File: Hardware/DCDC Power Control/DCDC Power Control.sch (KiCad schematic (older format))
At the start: 33 parts, among them J1 Conn_01x03, J2 Conn_01x02, J3 Conn_01x02, J4 Screw_Terminal_01x02, J5 Conn_01x01, Q2 SQJ479EP-T1_GE3, U1 CPC2025N

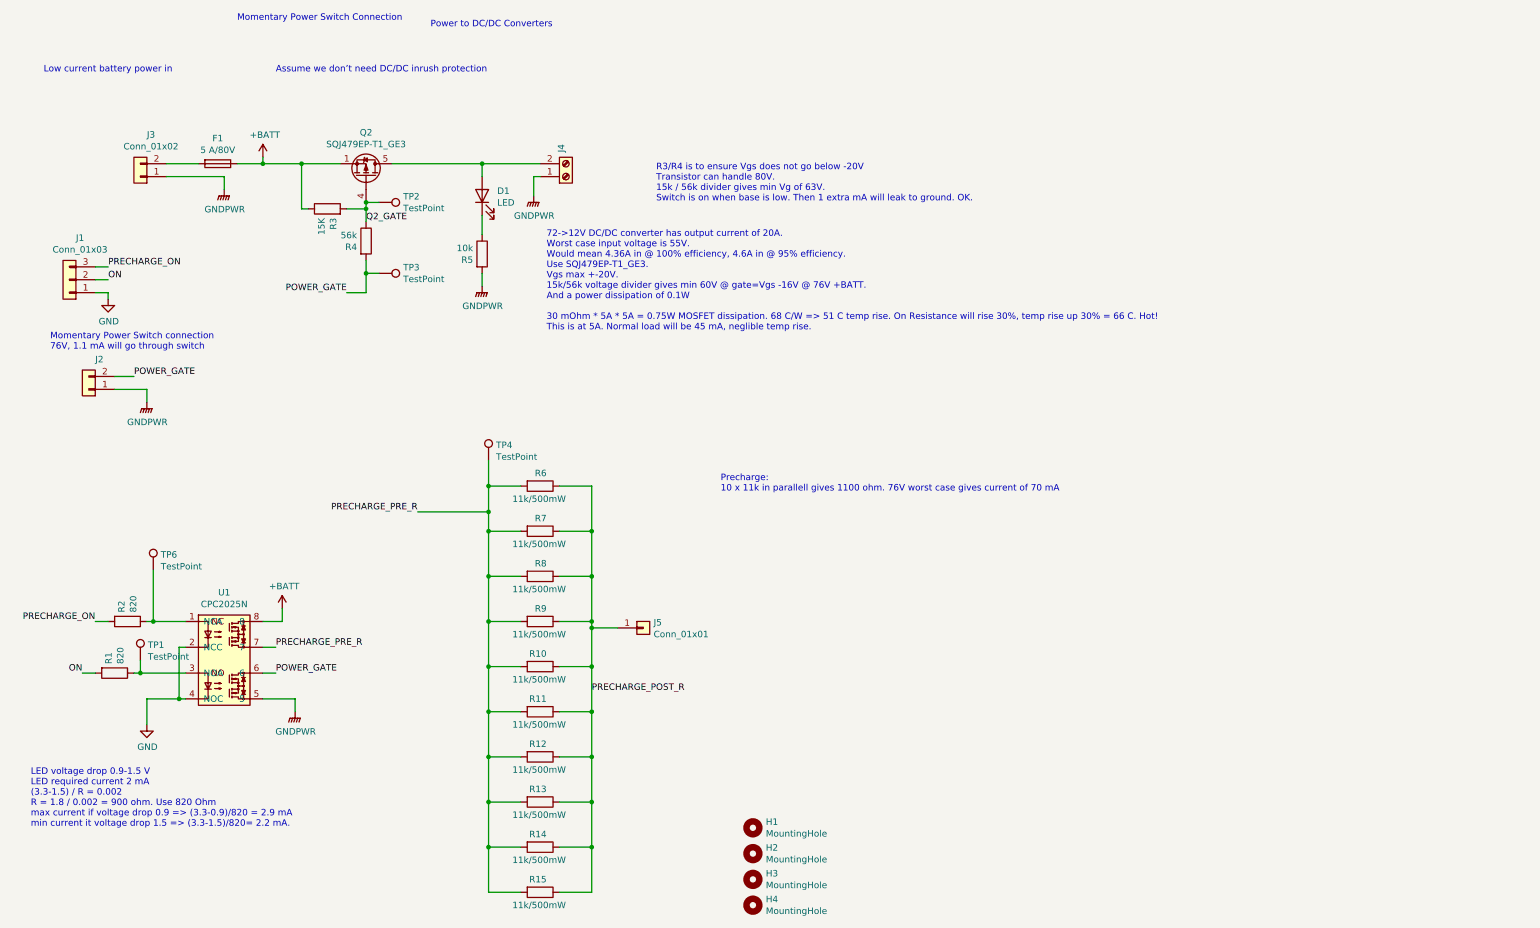
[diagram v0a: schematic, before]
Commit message: Revision 2 of the DCDC Control PCB.
Now with precharge for both DC/DC and VESC, 150 ohm 45 W precharge resistors
(up to three per device).

Microcontroller to control the sequencing. ADC measurement of in vs out voltage
to determine when precharge is complete.
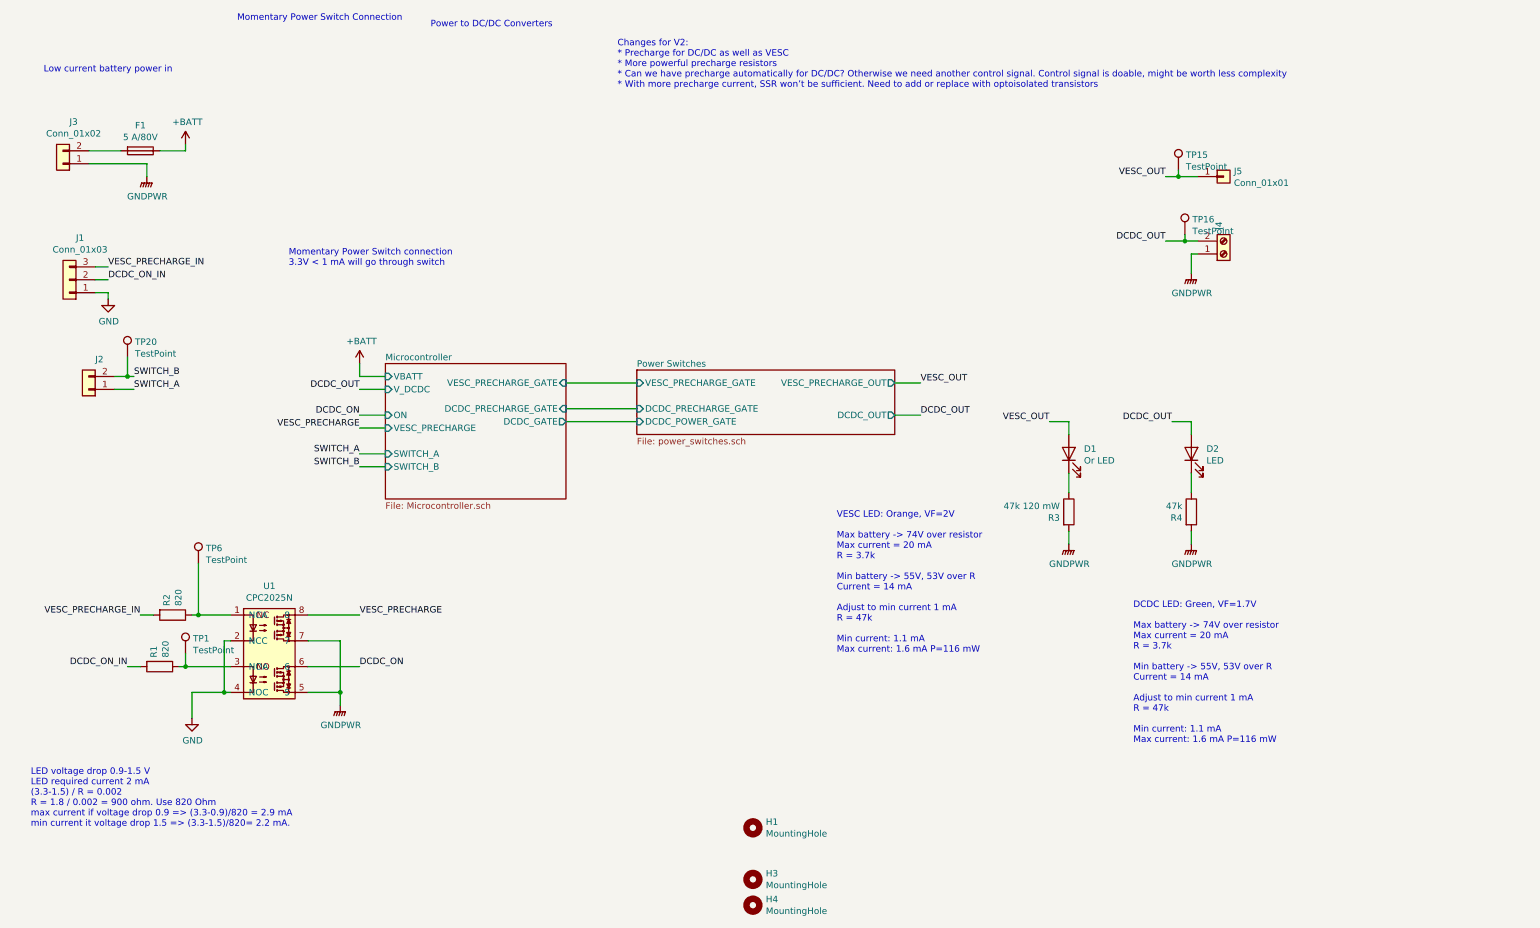
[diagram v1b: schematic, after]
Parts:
- removed H2: MountingHole, MountingHole:MountingHole_4.3mm_M4_ISO14580, symbol Mechanical:MountingHole
- removed Q2: SQJ479EP-T1_GE3, Package_SO:Vishay_PowerPAK_1212-8_Single, symbol Transistor_FET:SiS415DNT
- removed R10, R11, R12, R13, R14, R15, R6, R7, R8, R9: 11k/500mW, Resistor_SMD:R_1206_3216Metric_Pad1.42x1.75mm_HandSolder, symbol Device:R
- removed R5: 10k, Resistor_SMD:R_0603_1608Metric_Pad1.05x0.95mm_HandSolder, symbol Device:R
- removed TP2, TP3, TP4: TestPoint, TestPoint:TestPoint_Pad_D2.0mm, symbol Connector:TestPoint
- added D2: LED, LED_SMD:LED_0603_1608Metric_Pad1.05x0.95mm_HandSolder, symbol Device:LED
- added TP15, TP16, TP20: TestPoint, TestPoint:TestPoint_Loop_D2.50mm_Drill1.0mm_LowProfile, symbol Connector:TestPoint
- D1: value LED -> Or LED; PN (none) -> 475-2486-1-ND
- R3: value 15K -> 47k 120 mW
- R4: value 56k -> 47k
- TP1, TP6: footprint TestPoint:TestPoint_Pad_D2.0mm -> TestPoint:TestPoint_Loop_D2.50mm_Drill1.0mm_LowProfile
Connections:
- net PRECHARGE_PRE_R is gone; now on net GNDPWR: U1.7
- net +BATT: no longer R3.1, U1.8
- net GNDPWR: now also R3.2, R4.2; no longer J2.1 (Pin_1)
- net DCDC_OUT: now reaches J4.2 (Pin_2)
- net DCDC_OUT: now also D2.2 (A), TP16.1; no longer D1.2 (A)
- net at D1.1 (K): now also R3.1
- net ON renamed DCDC_ON_IN
- removed net POWER_GATE: J2.2 (Pin_2), R4.2, U1.6
- net PRECHARGE_ON renamed VESC_PRECHARGE_IN
- net PRECHARGE_POST_R renamed VESC_OUT
- net VESC_OUT: now also D1.2 (A), TP15.1
- net Q2_GATE: no longer names the net of R4.1
- net Q2_GATE: now also D2.1 (K); no longer R3.2
- new net DCDC_ON: U1.6
- new net SWITCH_A: J2.1 (Pin_1)
- new net SWITCH_B: J2.2 (Pin_2), TP20.1
- new net VESC_PRECHARGE: U1.8
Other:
- note added: "Changes for V2:\n* Precharge for DC/DC as well as VESC\n* More powerful precharge resistors\n* Can we have precharge automatically for DC/DC? Otherwise we need another control signal. Control signal is doable, might be worth less complexity\n* With more precharge current, SSR won’t be sufficient. Need to add or replace with optoisolated transistors\n\n"
- note added: "DCDC LED: Green, VF=1.7V\n\nMax battery -> 74V over resistor\nMax current = 20 mA\nR = 3.7k\n\nMin battery -> 55V, 53V over R\nCurrent = 14 mA\n\nAdjust to min current 1 mA\nR = 47k\n\nMin current: 1.1 mA\nMax current: 1.6 mA P=116 mW"
- note added: "Momentary Power Switch connection\n3.3V < 1 mA will go through switch"
- note added: "VESC LED: Orange, VF=2V\n\nMax battery -> 74V over resistor\nMax current = 20 mA\nR = 3.7k\n\nMin battery -> 55V, 53V over R\nCurrent = 14 mA\n\nAdjust to min current 1 mA\nR = 47k\n\nMin current: 1.1 mA\nMax current: 1.6 mA P=116 mW"
- note removed: "72->12V DC/DC converter has output current of 20A.\nWorst case input voltage is 55V. \nWould mean 4.36A in @ 100% efficiency, 4.6A in @ 95% efficiency.\nUse SQJ479EP-T1_GE3.\nVgs max +-20V. \n15k/56k voltage divider gives min 60V @ gate=Vgs -16V @ 76V +BATT. \nAnd a power dissipation of 0.1W\n\n30 mOhm * 5A * 5A = 0.75W MOSFET dissipation. 68 C/W => 51 C temp rise. On Resistance will rise 30%, te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"
- note removed: "Assume we don’t need DC/DC inrush protection"
- note removed: "Momentary Power Switch connection\n76V, 1.1 mA will go through switch"
- note removed: "Precharge:\n10 x 11k in parallell gives 1100 ohm. 76V worst case gives current of 70 mA\n"
- note removed: "R3/R4 is to ensure Vgs does not go below -20V\nTransistor can handle 80V.\n15k / 56k divider gives min Vg of 63V.\nSwitch is on when base is low. Then 1 extra mA will leak to ground. OK.\n"
- moved on the sheet: F1, J3, J4, J5, R1, R2, TP1, TP6, U1

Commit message: Older PCB updates
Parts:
- added TP21, TP22: TestPoint, TestPoint:TestPoint_Loop_D2.50mm_Drill1.0mm_LowProfile, symbol Connector:TestPoint
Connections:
- net GND: now also TP21.1
- net GNDPWR: now also TP22.1
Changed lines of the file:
@@
 Text Notes 800  1150 0    50   ~ 0
 Low current battery power in
-Text Notes 2300 750  0    50   ~ 0
+Text Notes 650  3750 0    50   ~ 0
 Momentary Power Switch Connection
 $Comp
@@
 Wire Wire Line
 	9700 2700 9700 2550
-Text Notes 3800 800  0    50   ~ 0
+Text Notes 9150 3050 0    50   ~ 0
 Power to DC/DC Converters
 Text Notes 2700 2650 0    50   ~ 0
@@
 $EndComp
 Wire Wire Line
-	1950 6150 1950 5950
+	1950 6150 1950 6050
 Wire Wire Line
 	1950 5950 2200 5950
@@
 Wire Wire Line
 	1450 3500 1500 3500
+$Comp
+L Connector:TestPoint TP21
+U 1 1 602EC0DF
+P 1500 6000
+F 0 "TP21" H 1558 6118 50  0000 L CNN
+F 1 "TestPoint" H 1558 6027 50  0000 L CNN
+F 2 "TestPoint:TestPoint_Loop_D2.50mm_Drill1.0mm_LowProfile" H 1700 6000 50  0001 C CNN
+F 3 "~" H 1700 6000 50  0001 C CNN
+	1    1500 6000
+	1    0    0    -1
+$EndComp
+Wire Wire Line
+	1500 6000 1500 6050
+Wire Wire Line
+	1500 6050 1950 6050
+Connection ~ 1950 6050
+Wire Wire Line
+	1950 6050 1950 5950
+$Comp
+L Connector:TestPoint TP22
+U 1 1 602EDF87
+P 2200 1800
+F 0 "TP22" H 2258 1918 50  0000 L CNN
+F 1 "TestPoint" H 2258 1827 50  0000 L CNN
+F 2 "TestPoint:TestPoint_Loop_D2.50mm_Drill1.0mm_LowProfile" H 2400 1800 50  0001 C CNN
+F 3 "~" H 2400 1800 50  0001 C CNN
+	1    2200 1800
+	1    0    0    -1
+$EndComp
+Wire Wire Line
+	1600 1850 2200 1850
+Wire Wire Line
+	2200 1850 2200 1800
+Connection ~ 1600 1850
 $EndSCHEMATC
